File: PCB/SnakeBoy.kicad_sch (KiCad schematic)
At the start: 22 parts, among them SW1 X, SW2 A, SW3 Y, SW4 B, SW5 Start, SW6 Select, SW7 Power_SW, U1 ESP32-S3-DEVKITC-1-N16R8, U2 Joystick, U4 TP4056 Module

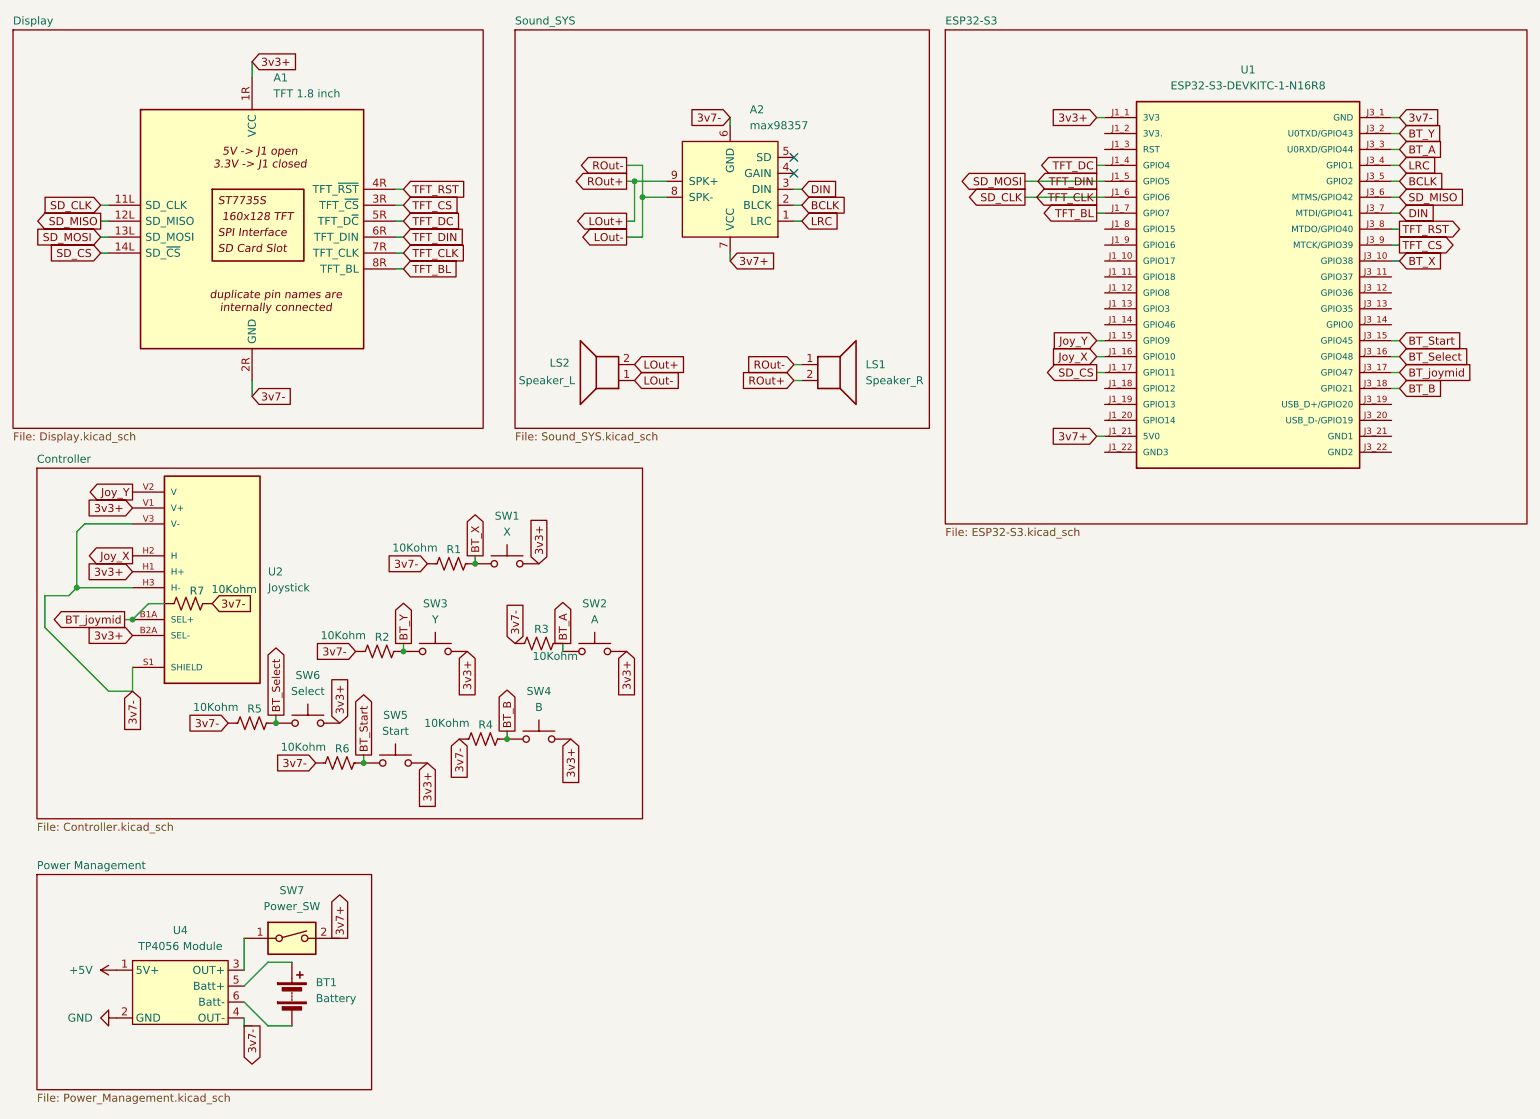
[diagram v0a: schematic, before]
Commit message: Added ILI9341 SPI Bigger TFT to the schem & Tid it up
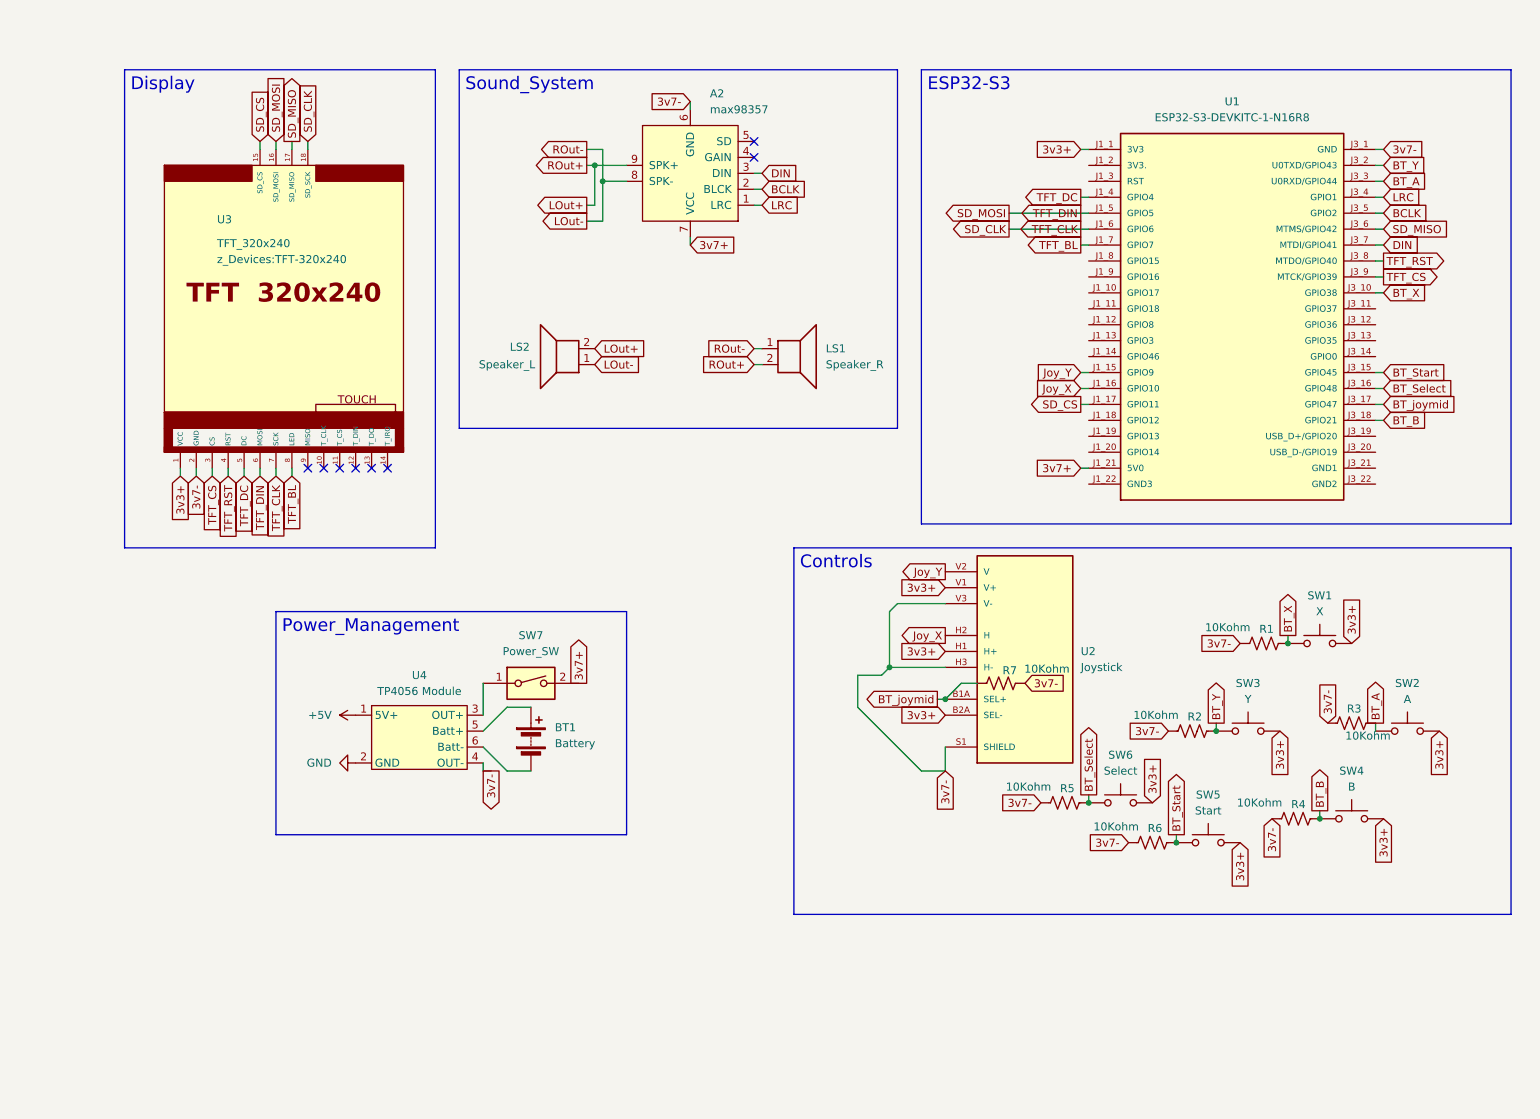
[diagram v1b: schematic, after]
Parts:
- removed A1: TFT 1.8 inch, Display-extra:Module_TFT_1.8_160x128, symbol Display_Graphic-extra:Module_TFT_1.8_160x128
- added U3: TFT_320x240, z_Devices:TFT-320x240, symbol tft:TFT_320x240
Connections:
- net 3v3+: now also U3.1 (VCC)
- net 3v7-: now also U3.2 (GND)
- net SD_CLK: now also U3.18 (SD_SCK), U3.7 (SCK)
- net SD_CS: now also U3.15 (SD_CS)
- net SD_MISO: now also U3.17 (SD_MISO)
- net SD_MOSI: now also U3.16 (SD_MOSI), U3.6 (MOSI)
- net TFT_BL: now also U3.8 (LED)
- net TFT_CS: now also U3.3 (CS)
- net TFT_DC: now also U3.5 (DC)
- net TFT_RST: now also U3.4 (RST)
- no-connect marks 2 -> 8
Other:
- removed sheet Controller
- removed sheet Display
- removed sheet ESP32-S3
- removed sheet Power Management
- removed sheet Sound_SYS
- moved on the sheet: A2, BT1, LS1, LS2, R1, R2, R3, R4, R5, R6, R7, SW1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

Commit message: Edited and Retraced the new screen
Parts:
- U3: footprint z_Devices:TFT-320x240 -> Display-extra:TFT-320x240
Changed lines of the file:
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@@
 			)
 		)
-		(property "Footprint" "z_Devices:TFT-320x240"
+		(property "Footprint" "Display-extra:TFT-320x240"
 			(at 50.292 55.626 0)
 			(show_name no)
